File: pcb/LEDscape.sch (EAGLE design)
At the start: 31 parts, among them IC1 MAX3041CUE, IC2 MAX3041CUE, IC3 MAX3041CUE, IC4 MAX3041CUE, IC5 MAX3041CUE, IC6 MAX3041CUE, IC7 MAX3041CUE, IC8 MAX3041CUE

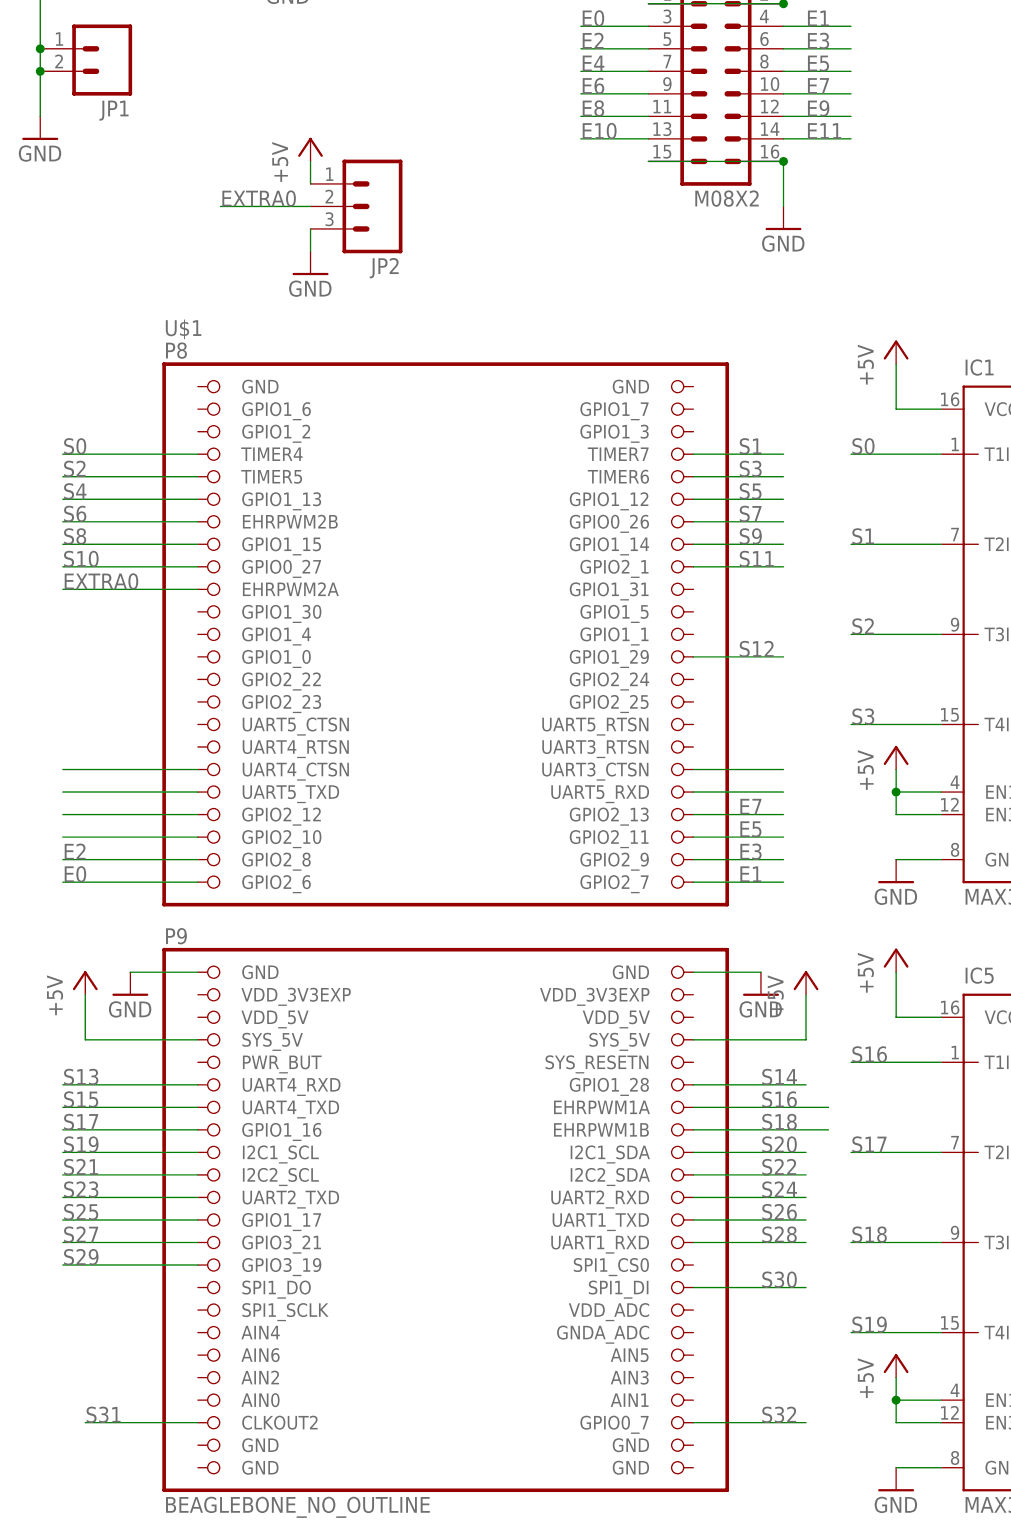
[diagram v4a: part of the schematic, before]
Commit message: Fix some ERC errors, a sad DRC one, and add an extra GPIO.
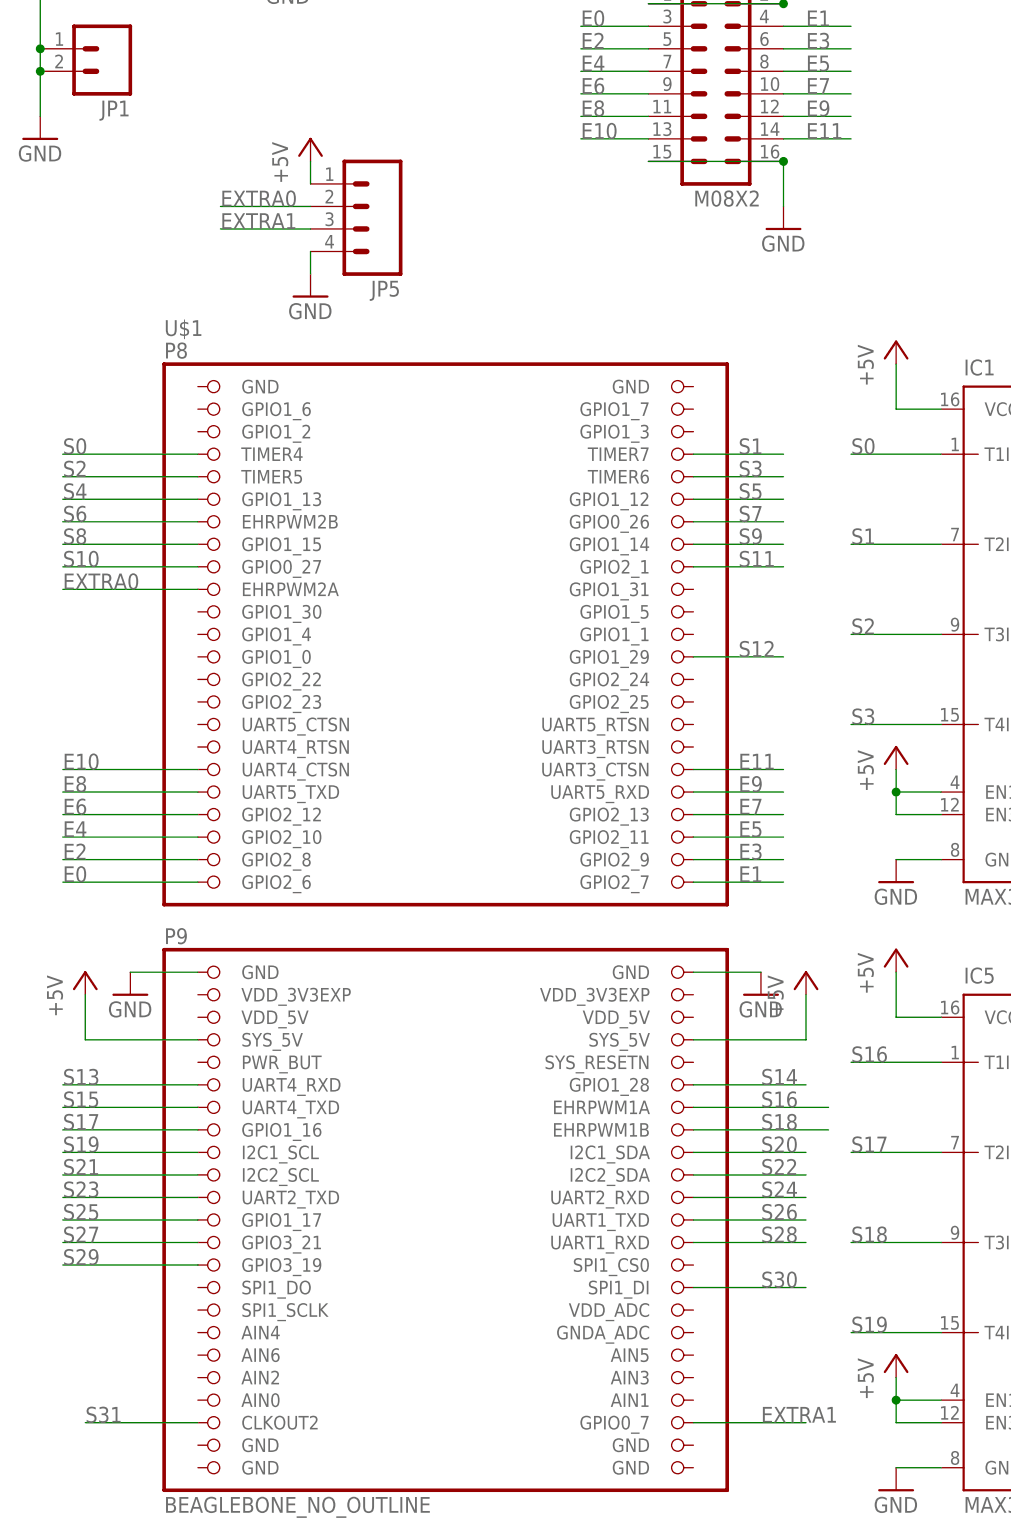
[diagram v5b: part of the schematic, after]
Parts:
- removed JP2: (no value), SparkFun-Connectors:M03PTH
- added JP5: (no value), SparkFun-Connectors:M041X04_NO_SILK
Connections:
- removed net S32: U$1.GPIO0_7
- new net EXTRA1: JP5.3, U$1.GPIO0_7
- net +5V: now also JP5.1; no longer JP2.1
- net EXTRA0: now also JP5.2; no longer JP2.2
- net GND: now also JP5.4; no longer JP2.3
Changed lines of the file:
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@@
 <part name="GND20" library="supply1" deviceset="GND" device=""/>
 <part name="GND21" library="supply1" deviceset="GND" device=""/>
-<part name="JP2" library="SparkFun-Connectors" deviceset="M03" device="PTH"/>
 <part name="GND22" library="supply1" deviceset="GND" device=""/>
 <part name="P+21" library="supply1" deviceset="+5V" device=""/>
@@
 <part name="P+22" library="supply1" deviceset="+5V" device=""/>
 <part name="GND23" library="supply1" deviceset="GND" device=""/>
+<part name="JP5" library="SparkFun-Connectors" deviceset="M04" device="1X04_NO_SILK"/>
 </parts>
 <sheets>
@@
 <instance part="GND20" gate="1" x="35.56" y="142.24"/>
 <instance part="GND21" gate="1" x="7.62" y="124.46"/>
-<instance part="JP2" gate="G$1" x="45.72" y="116.84" rot="R180"/>
-<instance part="GND22" gate="1" x="38.1" y="109.22"/>
+<instance part="GND22" gate="1" x="38.1" y="106.68"/>
 <instance part="P+21" gate="1" x="38.1" y="124.46"/>
 <instance part="U$12" gate="G$1" x="83.82" y="129.54"/>
 <instance part="P+22" gate="1" x="91.44" y="147.32"/>
 <instance part="GND23" gate="1" x="91.44" y="114.3"/>
+<instance part="JP5" gate="G$1" x="43.18" y="116.84" rot="R180"/>
 </instances>
 <busses>
@@
 </segment>
 <segment>
-<pinref part="JP2" gate="G$1" pin="1"/>
 <pinref part="P+21" gate="1" pin="+5V"/>
 <wire x1="38.1" y1="119.38" x2="38.1" y2="121.92" width="0.1524" layer="91"/>
+<pinref part="JP5" gate="G$1" pin="1"/>
 </segment>
 <segment>
@@
 </segment>
 <segment>
-<pinref part="JP2" gate="G$1" pin="3"/>
 <pinref part="GND22" gate="1" pin="GND"/>
-<wire x1="38.1" y1="114.3" x2="38.1" y2="111.76" width="0.1524" layer="91"/>
+<pinref part="JP5" gate="G$1" pin="4"/>
+<wire x1="38.1" y1="109.22" x2="38.1" y2="111.76" width="0.1524" layer="91"/>
 </segment>
 <segment>
@@
 </segment>
 </net>
-<net name="S32" class="0">
+<net name="EXTRA1" class="0">
 <segment>
 <pinref part="U$1" gate="G$1" pin="GPIO0_7"/>
 <wire x1="81.28" y1="-20.32" x2="93.98" y2="-20.32" width="0.1524" layer="91"/>
 <label x="88.9" y="-20.32" size="1.778" layer="95"/>
+</segment>
+<segment>
+<pinref part="JP5" gate="G$1" pin="3"/>
+<wire x1="38.1" y1="114.3" x2="27.94" y2="114.3" width="0.1524" layer="91"/>
+<label x="27.94" y="114.3" size="1.778" layer="95"/>
 </segment>
 </net>
@@
 </segment>
 <segment>
-<pinref part="JP2" gate="G$1" pin="2"/>
 <wire x1="38.1" y1="116.84" x2="27.94" y2="116.84" width="0.1524" layer="91"/>
 <label x="27.94" y="116.84" size="1.778" layer="95"/>
+<pinref part="JP5" gate="G$1" pin="2"/>
 </segment>
 </net>
@@
 <pinref part="U$1" gate="G$1" pin="GPIO2_10"/>
 <wire x1="10.16" y1="45.72" x2="25.4" y2="45.72" width="0.1524" layer="91"/>
+<label x="10.16" y="45.72" size="1.778" layer="95"/>
 </segment>
 </net>
@@
 <pinref part="U$1" gate="G$1" pin="GPIO2_12"/>
 <wire x1="25.4" y1="48.26" x2="10.16" y2="48.26" width="0.1524" layer="91"/>
+<label x="10.16" y="48.26" size="1.778" layer="95"/>
 </segment>
 </net>
@@
 <pinref part="U$1" gate="G$1" pin="UART5_TXD"/>
 <wire x1="10.16" y1="50.8" x2="25.4" y2="50.8" width="0.1524" layer="91"/>
+<label x="10.16" y="50.8" size="1.778" layer="95"/>
 </segment>
 </net>
@@
 <pinref part="U$1" gate="G$1" pin="UART4_CTSN"/>
 <wire x1="25.4" y1="53.34" x2="10.16" y2="53.34" width="0.1524" layer="91"/>
+<label x="10.16" y="53.34" size="1.778" layer="95"/>
 </segment>
 </net>
@@
 <pinref part="U$1" gate="G$1" pin="UART5_RXD"/>
 <wire x1="81.28" y1="50.8" x2="91.44" y2="50.8" width="0.1524" layer="91"/>
+<label x="86.36" y="50.8" size="1.778" layer="95"/>
 </segment>
 </net>
@@
 <pinref part="U$1" gate="G$1" pin="UART3_CTSN"/>
 <wire x1="81.28" y1="53.34" x2="91.44" y2="53.34" width="0.1524" layer="91"/>
+<label x="86.36" y="53.34" size="1.778" layer="95"/>
 </segment>
 </net>
@@
 </sheet>
 </sheets>
+<errors>
+</errors>
 </schematic>
 </drawing>
